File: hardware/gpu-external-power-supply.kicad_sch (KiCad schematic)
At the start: 0 parts

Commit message: chore: remove computer control and clean global references
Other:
- removed sheet Computer Control
- sheet 12V Supply ports: added none; removed otsd_12v_spply_dcpwr
- sheet Onboard Control ports: added none; removed onbrd_cntrl_cntrllr_dsig, otsd_onbrd_cntrl_usrin
- sheet U Controller ports: added none; removed cmptr_ntrfc_u_cntrllr_data, lw_crrnt_spply_u_cntrllr_dcpwr, onbrd_cntrl_u_cntrllr_dsig, u_cntrllr_vrm_cntrllr_data, u_cntrllr_vrm_cntrllr_dsig
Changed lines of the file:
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@@
-			)
-		)
-		(pin "cmptr_ntrfc_u_cntrllr_data" input
-			(at 19.05 130.81 180)
-			(effects
-				(font
-					(size 1.27 1.27)
-				)
-				(justify left)
-			)
-		)
-		(pin "onbrd_cntrl_u_cntrllr_dsig" input
-			(at 19.05 134.62 180)
-			(effects
-				(font
-					(size 1.27 1.27)
-				)
-				(justify left)
-			)
-		)
-		(pin "lw_crrnt_spply_u_cntrllr_dcpwr" input
-			(at 19.05 138.43 180)
-			(effects
-				(font
-					(size 1.27 1.27)
-				)
-				(justify left)
-			)
-		)
-		(pin "u_cntrllr_vrm_cntrllr_data" input
-			(at 80.01 137.16 0)
-			(effects
-				(font
-					(size 1.27 1.27)
-				)
-				(justify right)
-			)
-		)
-		(pin "u_cntrllr_vrm_cntrllr_dsig" input
-			(at 80.01 133.35 0)
-			(effects
-				(font
-					(size 1.27 1.27)
-				)
-				(justify right)
 			)
 		)
@@
 			)
 		)
-		(pin "otsd_onbrd_cntrl_usrin" input
-			(at 21.59 30.48 180)
-			(effects
-				(font
-					(size 1.27 1.27)
-				)
-				(justify left)
-			)
-		)
-		(pin "onbrd_cntrl_cntrllr_dsig" input
-			(at 78.74 30.48 0)
-			(effects
-				(font
-					(size 1.27 1.27)
-				)
-				(justify right)
-			)
-		)
 		(instances
 			(project "gpu-external-power-supply"
@@
 	)
 	(sheet
-		(at 21.59 46.99)
-		(size 54.61 17.78)
-		(fields_autoplaced yes)
-		(stroke
-			(width 0.1524)
-			(type solid)
-		)
-		(fill
-			(color 0 0 0 0.0000)
-		)
-		(property "Sheetname" "Computer Control"
-			(at 21.59 46.2784 0)
-			(effects
-				(font
-					(size 1.27 1.27)
-				)
-				(justify left bottom)
-			)
-		)
-		(property "Sheetfile" "Computer_Control.kicad_sch"
-			(at 21.59 65.3546 0)
-			(effects
-				(font
-					(size 1.27 1.27)
-				)
-				(justify left top)
-			)
-		)
-		(pin "otsd_cmptr_ntrfc_data" input
-			(at 21.59 49.53 180)
-			(effects
-				(font
-					(size 1.27 1.27)
-				)
-				(justify left)
-			)
-		)
-		(pin "otsd_cmptr_ntrfc_usrin" input
-			(at 21.59 54.61 180)
-			(effects
-				(font
-					(size 1.27 1.27)
-				)
-				(justify left)
-			)
-		)
-		(pin "cmptr_ntrfc_u_cntrllr_data" input
-			(at 76.2 55.88 0)
-			(effects
-				(font
-					(size 1.27 1.27)
-				)
-				(justify right)
-			)
-		)
-		(pin "otsd_cmptr_ntrfc_usrout" input
-			(at 21.59 59.69 180)
-			(effects
-				(font
-					(size 1.27 1.27)
-				)
-				(justify left)
-			)
-		)
-		(instances
-			(project "gpu-external-power-supply"
-				(path "/d5303413-7068-41ba-88e3-39dfa38d31b7"
-					(page "10")
-				)
-			)
-		)
-	)
-	(sheet
 		(at 250.19 110.49)
 		(size 30.48 13.97)
@@
 			)
 		)
-		(pin "otsd_12v_spply_dcpwr" input
-			(at 21.59 83.82 180)
-			(effects
-				(font
-					(size 1.27 1.27)
-				)
-				(justify left)
-			)
-		)

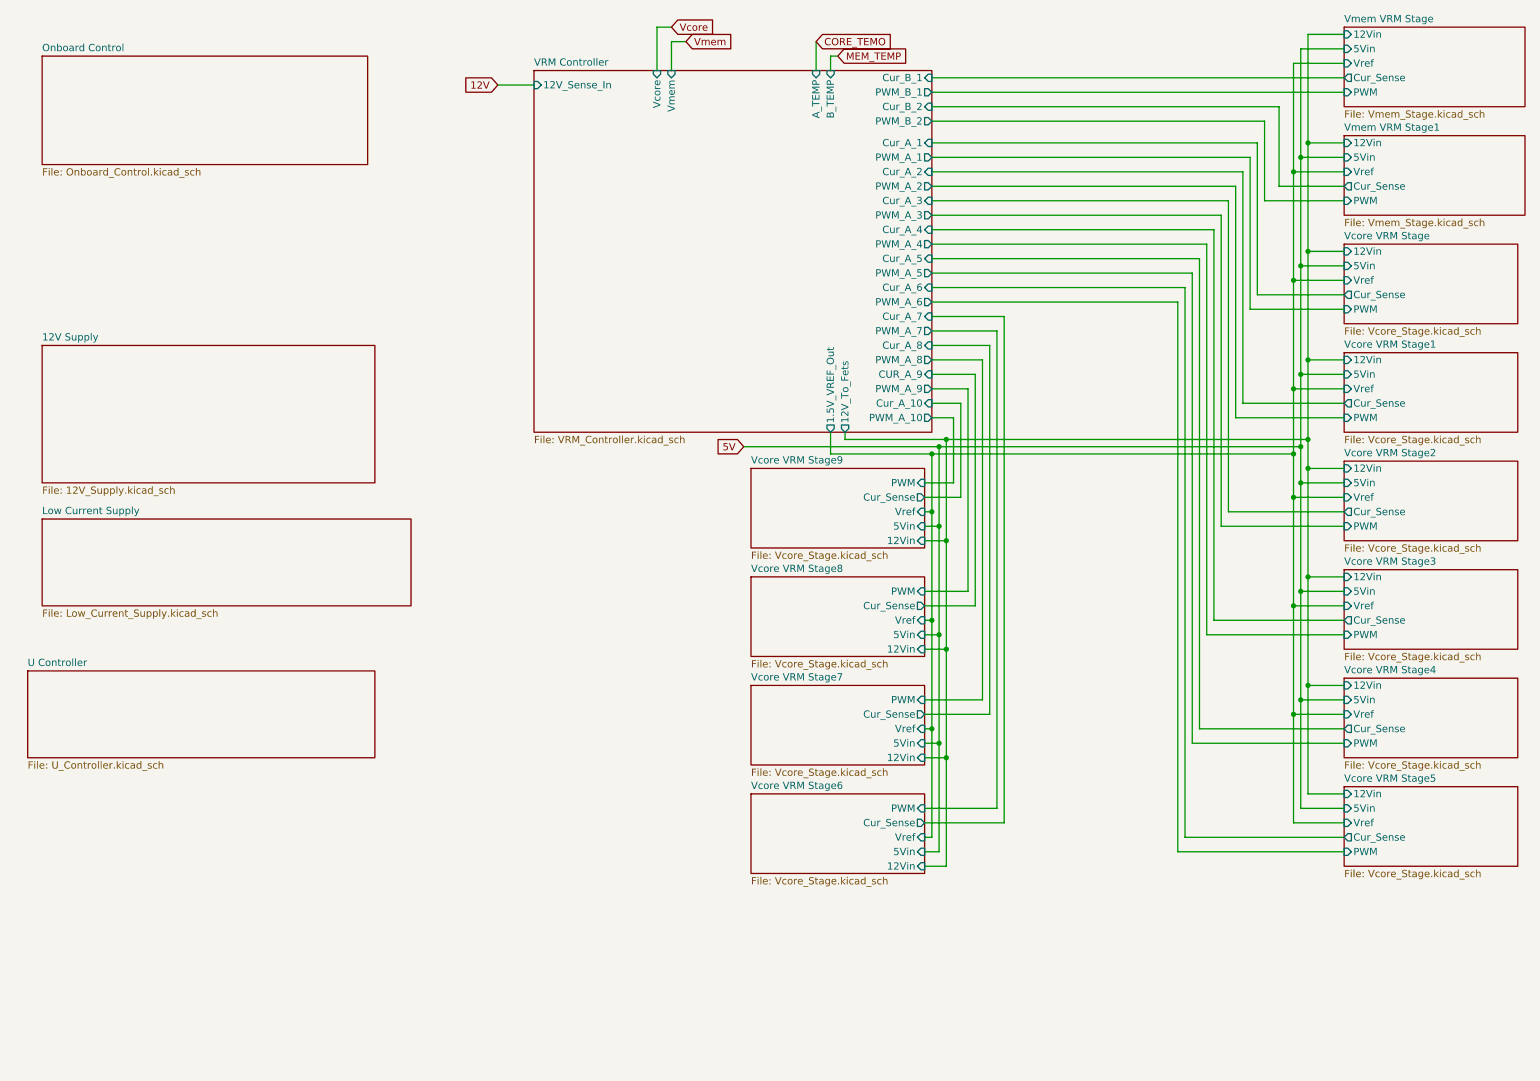
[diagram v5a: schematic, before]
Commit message: feat(schematic): refactor main heirarchy
This commit makes a bunch of changes to how power is delivered on the
schematic. It also adds the probit header and the i2c output connector
on the main page of the schematic. Lastly, it changes it so that USB
power should work and also not power the 5V rail to the mosfet ICs.
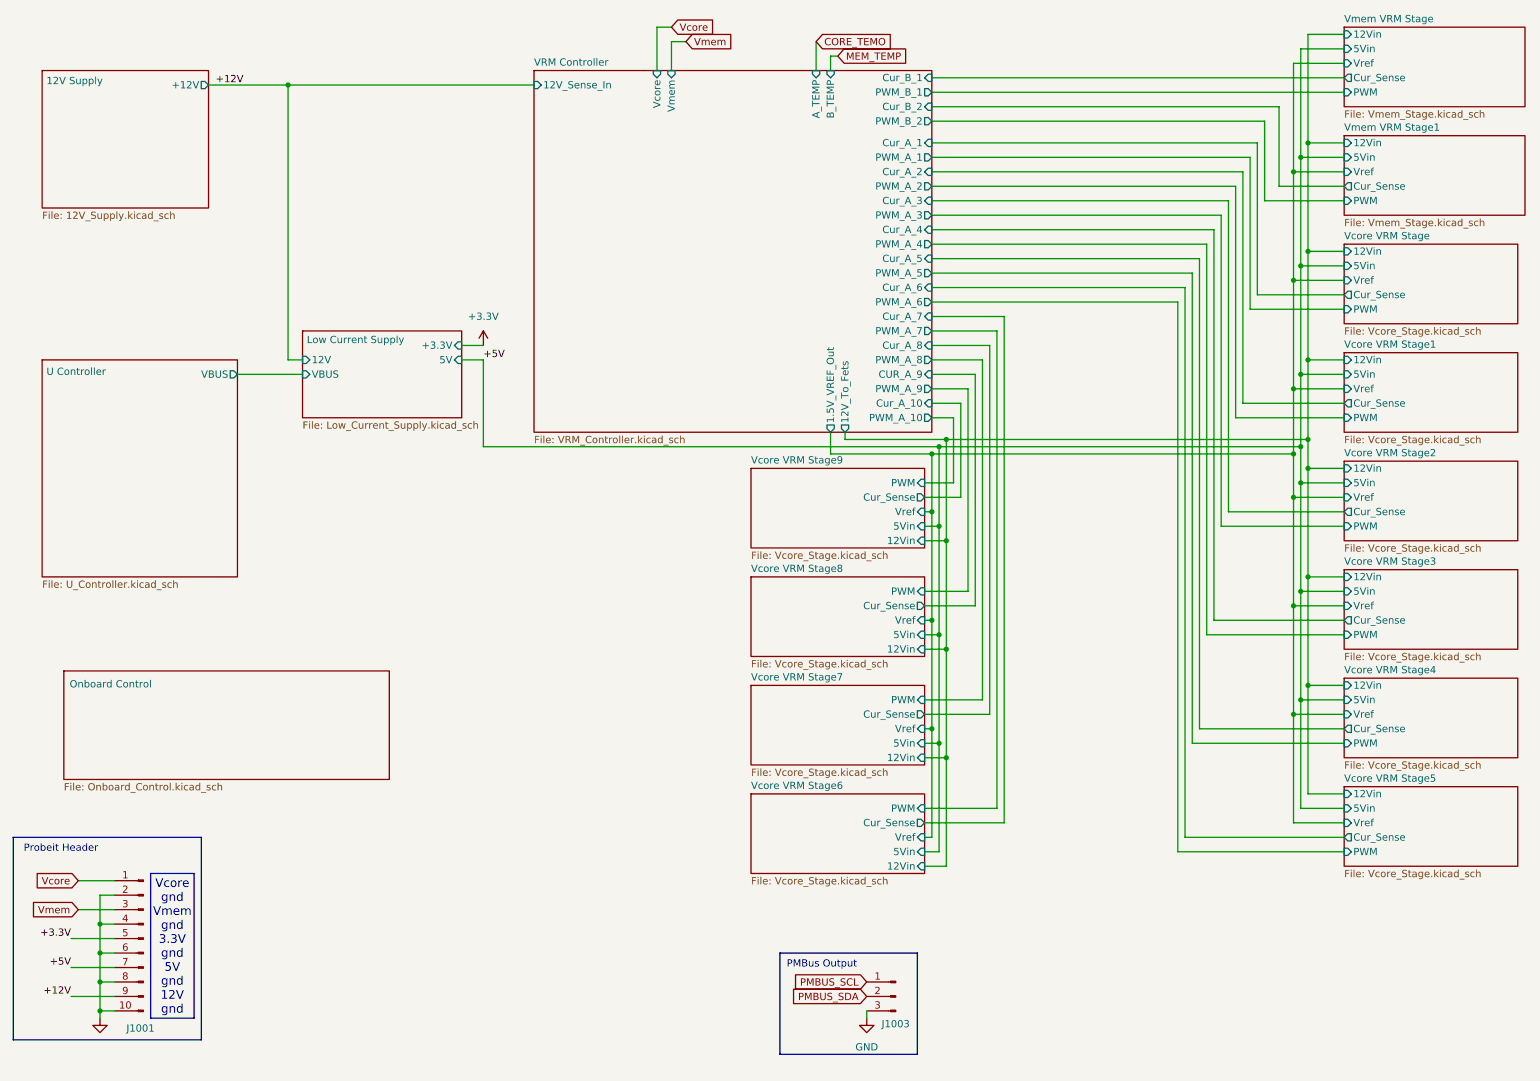
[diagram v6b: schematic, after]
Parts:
- added J1001: Conn_01x10_Pin, symbol Connector:Conn_01x10_Pin
- added J1003: Conn_01x03_Pin, Connector_PinHeader_2.54mm:PinHeader_1x03_P2.54mm_Vertical_SMD_Pin1Left, symbol Connector:Conn_01x03_Pin
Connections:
- net Vcore: now also J1001.1 (Pin_1)
- net Vmem: now also J1001.3 (Pin_3)
- new net +12V: J1001.9 (Pin_9)
- new net +3.3V: J1001.5 (Pin_5)
- new net +5V: J1001.7 (Pin_7)
- new net GND: J1001.10 (Pin_10), J1001.2 (Pin_2), J1001.4 (Pin_4), J1001.6 (Pin_6), J1001.8 (Pin_8), J1003.3 (Pin_3)
- new net PMBUS_SCL: J1003.1 (Pin_1)
- new net PMBUS_SDA: J1003.2 (Pin_2)
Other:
- sheet 12V Supply ports: added +12V; removed none
- sheet Low Current Supply ports: added +3.3V, 12V, 5V, VBUS; removed none
- sheet U Controller ports: added VBUS; removed none
- note added: "PMBus Output"
- note added: "Probeit Header"
- note added: "Vcore gnd Vmem gnd 3.3V gnd 5V gnd 12V gnd"

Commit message: feat(schematic): added cooler mounting holes
added cooler mounting holes to schematic
changed temp pins to read proper tempurature
small fixes
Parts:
- added H1, H2, H3, H4: MountingHole_Pad, MountingHole:MountingHole_2.2mm_M2_Pad, symbol Mechanical:MountingHole_Pad
- J1001: footprint (none) -> Connector_JST:JST_PH_S10B-PH-K_1x10_P2.00mm_Horizontal
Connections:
- net +12V: no longer J1001.9 (Pin_9)
- net GND: now also H1.1, H2.1, H3.1, H4.1
- new net CSNIN: J1001.9 (Pin_9)
